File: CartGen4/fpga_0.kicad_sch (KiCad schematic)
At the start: 12 parts, among them U9 LFXP2-8E-5MN132C

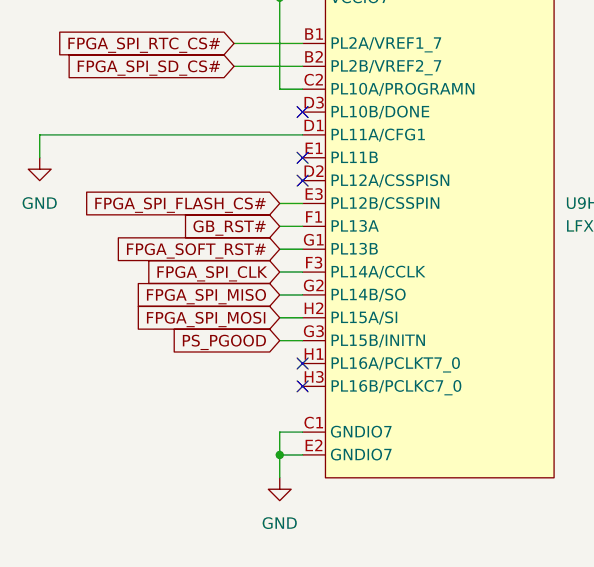
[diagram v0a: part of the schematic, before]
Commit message: Wired SPI bus
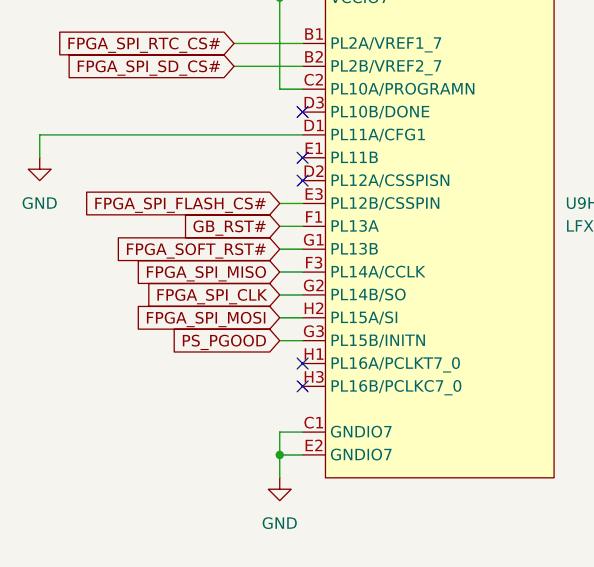
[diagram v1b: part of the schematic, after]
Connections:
- net FPGA_SPI_CLK: now also U9.G2 (PL14B/SO); no longer U9.F3 (PL14A/CCLK)
- net FPGA_SPI_MISO: now also U9.F3 (PL14A/CCLK); no longer U9.G2 (PL14B/SO)
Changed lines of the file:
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@@
+    )
+  )
+  (global_label "FPGA_SPI_CLK" (shape input) (at 53.34 82.55 180) (fields_autoplaced)
+    (effects (font (size 1.27 1.27)) (justify right))
+    (property "Intersheet References" "${INTERSHEET_REFS}" (id 0) (at 37.6221 82.4706 0)
+      (effects (font (size 1.27 1.27)) (justify right) hide)
     )
   )
@@
     )
   )
-  (global_label "FPGA_SPI_CLK" (shape input) (at 53.34 80.01 180) (fields_autoplaced)
-    (effects (font (size 1.27 1.27)) (justify right))
-    (property "Intersheet References" "${INTERSHEET_REFS}" (id 0) (at 37.6221 79.9306 0)
-      (effects (font (size 1.27 1.27)) (justify right) hide)
-    )
-  )
   (global_label "FPGA_SPI_FLASH_CS#" (shape input) (at 53.34 72.39 180) (fields_autoplaced)
     (effects (font (size 1.27 1.27)) (justify right))
@@
     )
   )
+  (global_label "FPGA_SPI_MISO" (shape input) (at 53.34 80.01 180) (fields_autoplaced)
+    (effects (font (size 1.27 1.27)) (justify right))
+    (property "Intersheet References" "${INTERSHEET_REFS}" (id 0) (at 36.594 79.9306 0)
+      (effects (font (size 1.27 1.27)) (justify right) hide)
+    )
+  )
   (global_label "RAM_ADV#" (shape input) (at 143.51 48.26 180) (fields_autoplaced)
     (effects (font (size 1.27 1.27)) (justify right))
@@
     (effects (font (size 1.27 1.27)) (justify right))
     (property "Intersheet References" "${INTERSHEET_REFS}" (id 0) (at 205.0807 65.9606 0)
-      (effects (font (size 1.27 1.27)) (justify right) hide)
-    )
-  )
-  (global_label "FPGA_SPI_MISO" (shape input) (at 53.34 82.55 180) (fields_autoplaced)
-    (effects (font (size 1.27 1.27)) (justify right))
-    (property "Intersheet References" "${INTERSHEET_REFS}" (id 0) (at 36.594 82.4706 0)
       (effects (font (size 1.27 1.27)) (justify right) hide)
     )
@@
   (symbol (lib_id "power:+1V2") (at 139.7 123.19 0) (unit 1)
     (in_bom yes) (on_board yes) (fields_autoplaced)
-    (property "Reference" "#PWR?" (id 0) (at 139.7 127 0)
+    (property "Reference" "#PWR0103" (id 0) (at 139.7 127 0)
       (effects (font (size 1.27 1.27)) hide)
     )
@@
   (symbol (lib_id "power:+3V3") (at 214.63 123.19 0) (unit 1)
     (in_bom yes) (on_board yes) (fields_autoplaced)
-    (property "Reference" "#PWR?" (id 0) (at 214.63 127 0)
+    (property "Reference" "#PWR0106" (id 0) (at 214.63 127 0)
       (effects (font (size 1.27 1.27)) hide)
     )
@@
   (symbol (lib_id "power:GND") (at 198.12 140.97 0) (unit 1)
     (in_bom yes) (on_board yes) (fields_autoplaced)
-    (property "Reference" "#PWR?" (id 0) (at 198.12 147.32 0)
+    (property "Reference" "#PWR0104" (id 0) (at 198.12 147.32 0)
       (effects (font (size 1.27 1.27)) hide)
     )
@@
   (symbol (lib_id "power:+1V8") (at 185.42 123.19 0) (unit 1)
     (in_bom yes) (on_board yes) (fields_autoplaced)
-    (property "Reference" "#PWR?" (id 0) (at 185.42 127 0)
+    (property "Reference" "#PWR0105" (id 0) (at 185.42 127 0)
       (effects (font (size 1.27 1.27)) hide)
     )
@@
   (symbol (lib_id "power:GND") (at 265.43 140.97 0) (unit 1)
     (in_bom yes) (on_board yes) (fields_autoplaced)
-    (property "Reference" "#PWR?" (id 0) (at 265.43 147.32 0)
-      (effects (font (size 1.27 1.27)) hide)
-    )
+    (property "Reference" "#PWR0107" (id 0) (at 265.43 147.32 0)
+      (effects (font (size 1.27 1.27)) hide)
+    )

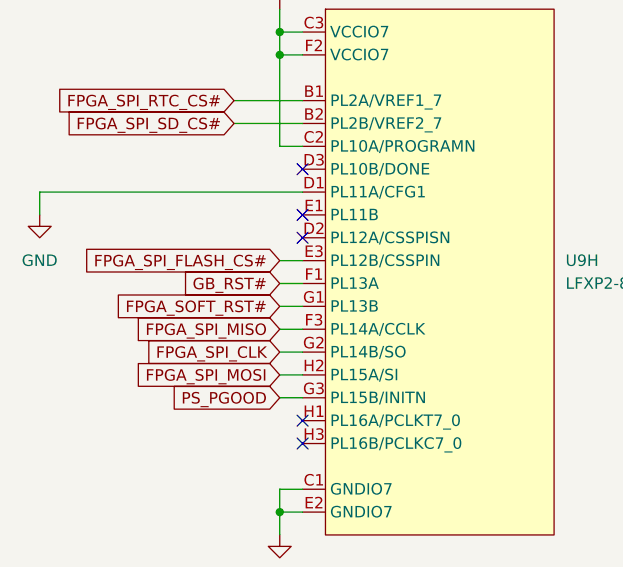
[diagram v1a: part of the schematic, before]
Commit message: Wired general purpose signals
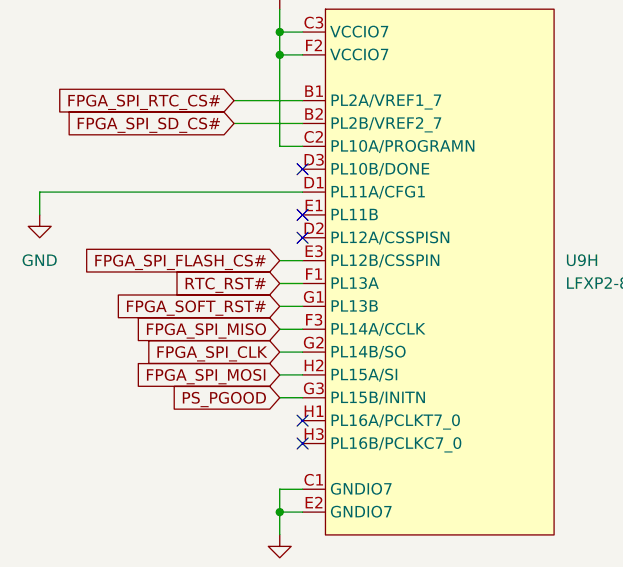
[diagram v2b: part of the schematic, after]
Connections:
- net GB_RST# renamed RTC_RST#
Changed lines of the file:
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@@
-    )
-  )
-  (global_label "GB_RST#" (shape input) (at 53.34 74.93 180) (fields_autoplaced)
-    (effects (font (size 1.27 1.27)) (justify right))
-    (property "Intersheet References" "${INTERSHEET_REFS}" (id 0) (at 42.7021 75.0094 0)
-      (effects (font (size 1.27 1.27)) (justify right) hide)
     )
   )
@@
       (effects (font (size 1.27 1.27)) (justify right) hide)
     )
+  )
+  (global_label "RTC_RST#" (shape input) (at 53.34 74.93 180) (fields_autoplaced)
+    (effects (font (size 1.27 1.27)) (justify right))
+    (property "Intersheet References" "${INTERSHEET_REFS}" (id 0) (at 41.7345 74.8506 0)
+      (effects (font (size 1.27 1.27)) (justify right) hide)
+    )

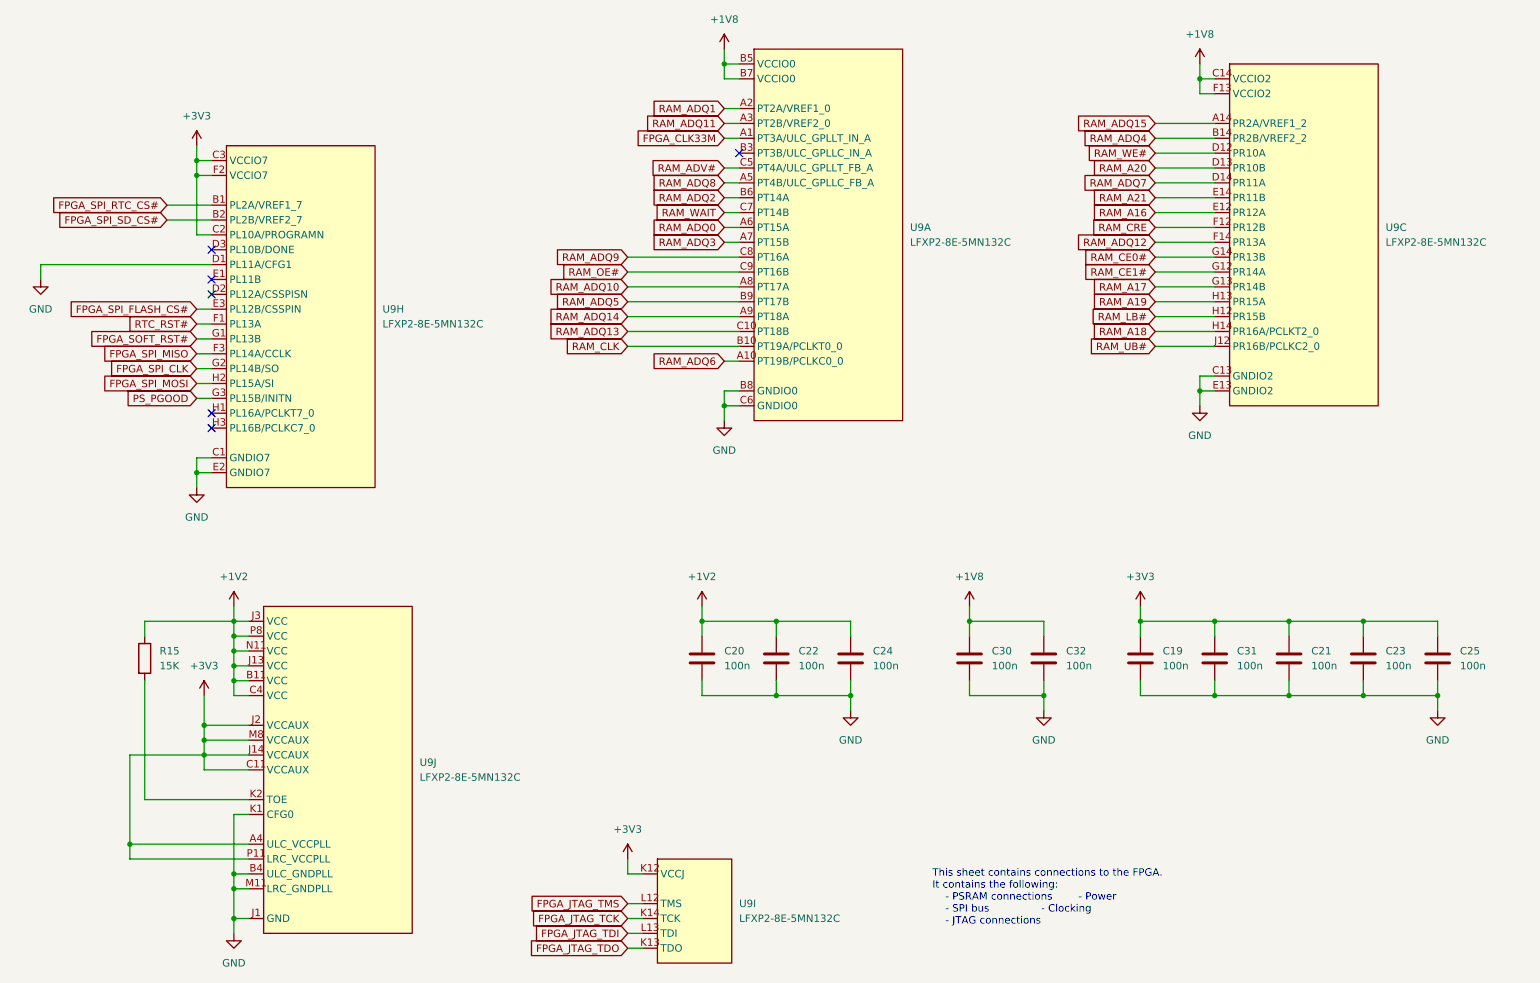
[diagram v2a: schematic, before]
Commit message: Rerouted some RAM and GB CTRL traces
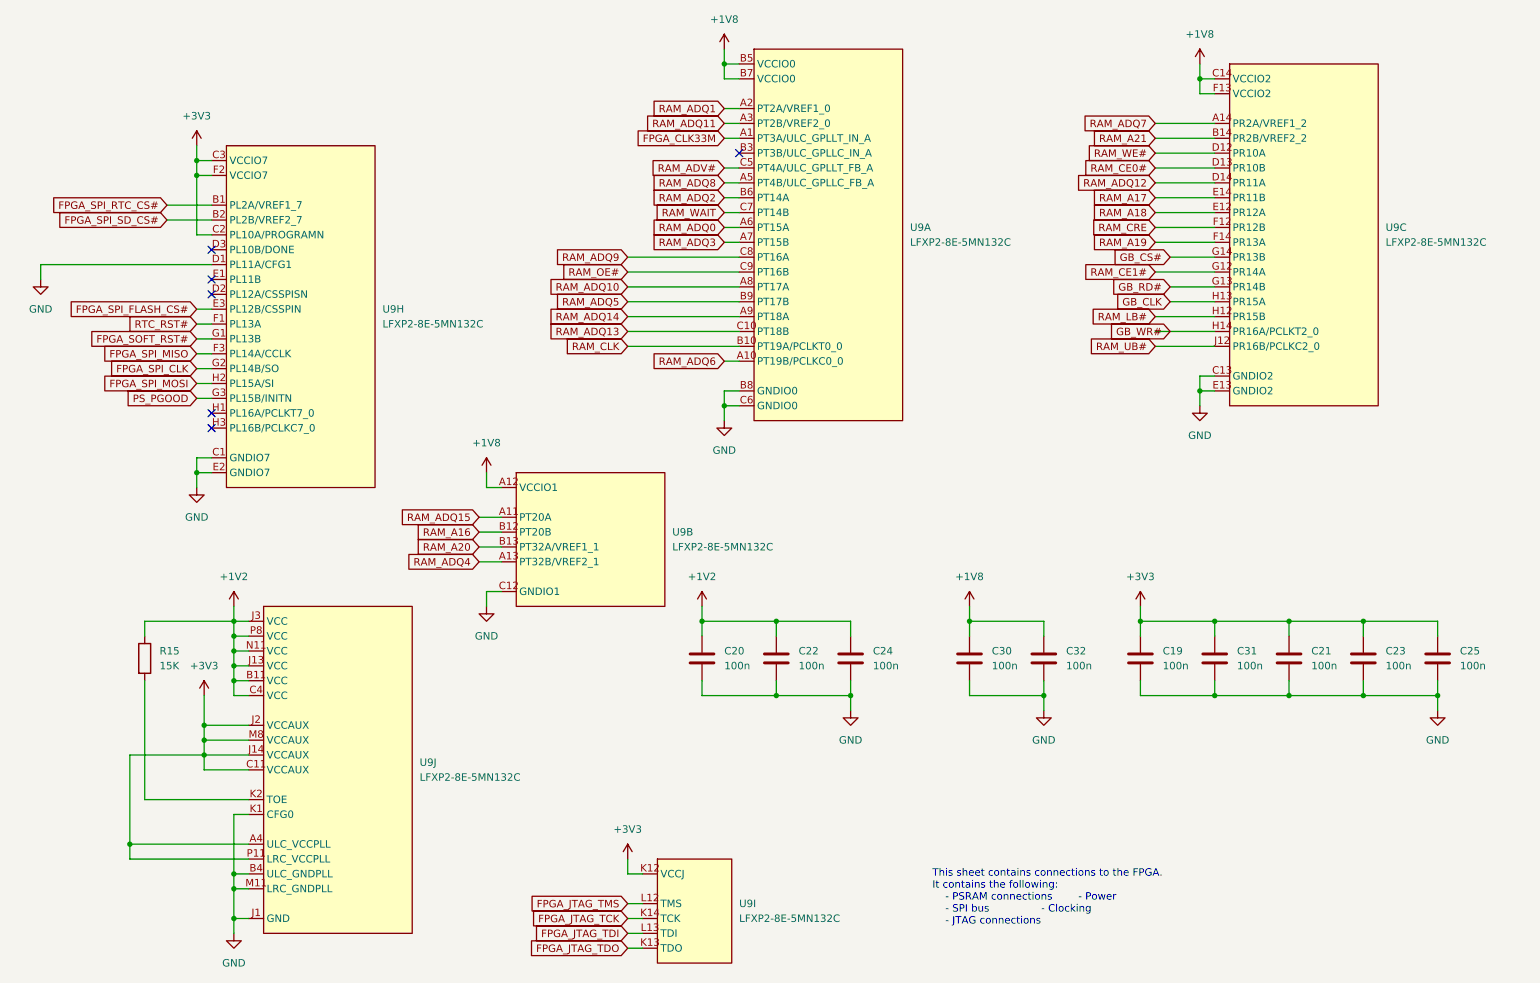
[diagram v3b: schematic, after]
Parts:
- added unit 2 of U9
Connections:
- net +1V8: now also U9.A12 (VCCIO1)
- net GND: now also U9.C12 (GNDIO1)
- net RAM_A16: now also U9.B12 (PT20B); no longer U9.E12 (PR12A)
- net RAM_A17: now also U9.E14 (PR11B); no longer U9.G13 (PR14B)
- net RAM_A18: now also U9.E12 (PR12A); no longer U9.H14 (PR16A/PCLKT2_0)
- net RAM_A19: now also U9.F14 (PR13A); no longer U9.H13 (PR15A)
- net RAM_A20: now also U9.B13 (PT32A/VREF1_1); no longer U9.D13 (PR10B)
- net RAM_A21: now also U9.B14 (PR2B/VREF2_2); no longer U9.E14 (PR11B)
- net RAM_ADQ12: now also U9.D14 (PR11A); no longer U9.F14 (PR13A)
- net RAM_ADQ15: now also U9.A11 (PT20A); no longer U9.A14 (PR2A/VREF1_2)
- net RAM_ADQ4: now also U9.A13 (PT32B/VREF2_1); no longer U9.B14 (PR2B/VREF2_2)
- net RAM_ADQ7: now also U9.A14 (PR2A/VREF1_2); no longer U9.D14 (PR11A)
- net RAM_CE0#: now also U9.D13 (PR10B); no longer U9.G14 (PR13B)
- new net GB_CLK: U9.H13 (PR15A)
- new net GB_CS#: U9.G14 (PR13B)
- new net GB_RD#: U9.G13 (PR14B)
- new net GB_WR#: U9.H14 (PR16A/PCLKT2_0)

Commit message: Added external test header to schematic
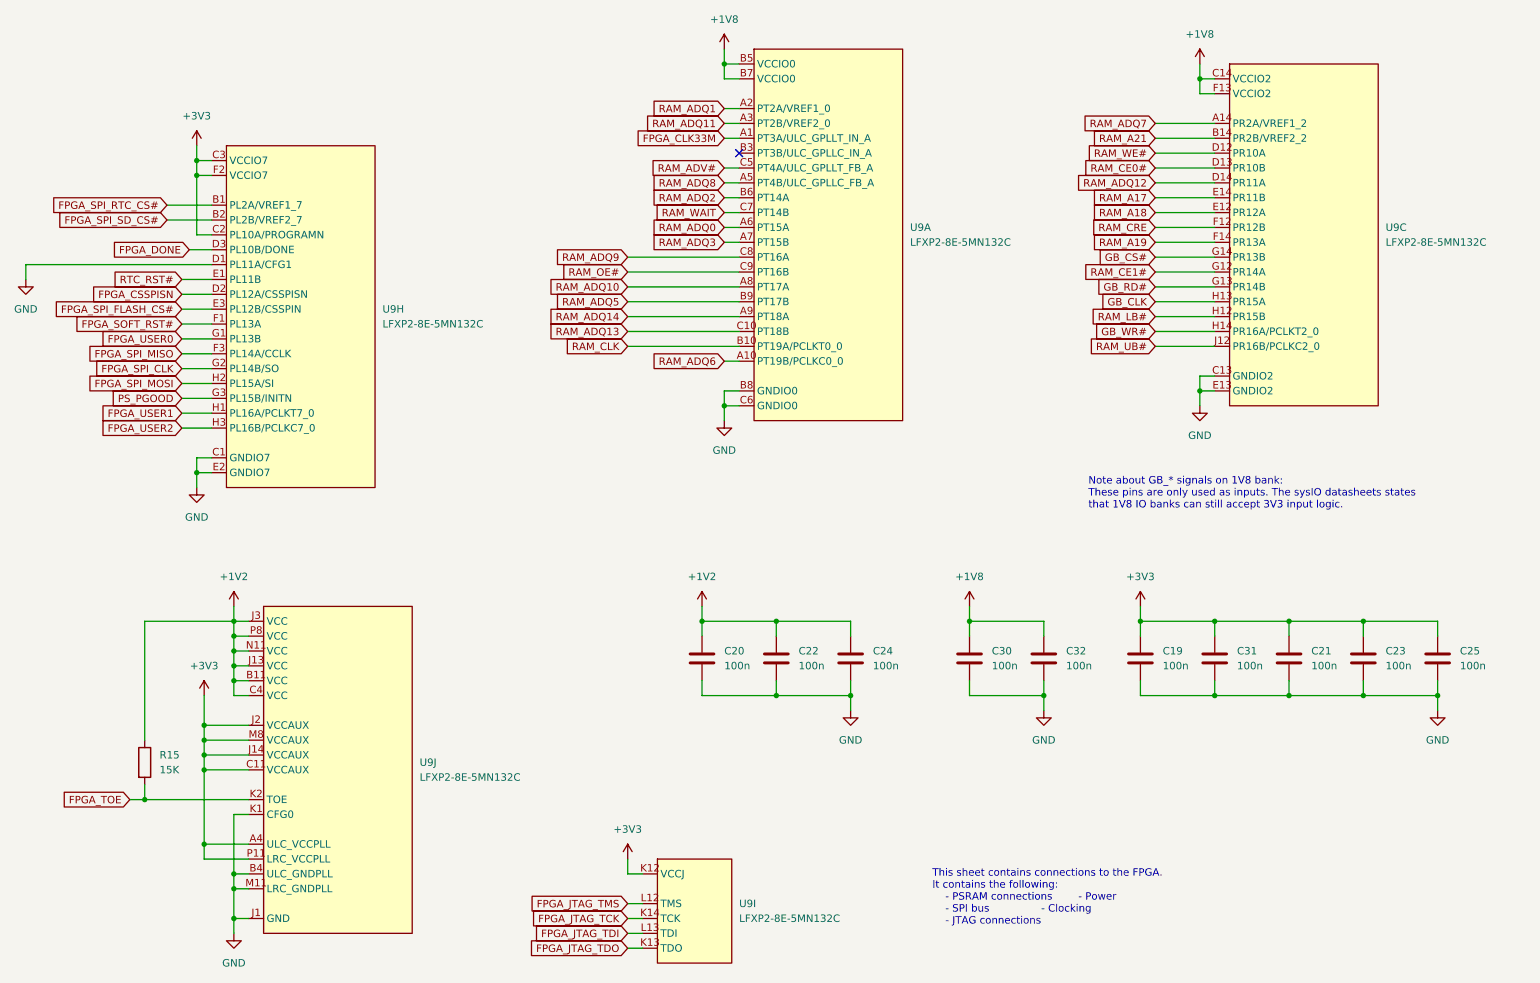
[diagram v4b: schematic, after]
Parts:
- removed unit 2 of U9
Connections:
- net FPGA_SOFT_RST#: now also U9.F1 (PL13A); no longer U9.G1 (PL13B)
- net RTC_RST#: now also U9.E1 (PL11B); no longer U9.F1 (PL13A)
- net FPGA_TOE: now reaches R15.2, U9.K2 (TOE)
- net FPGA_CSSPISN: now reaches U9.D2 (PL12A/CSSPISN)
- net FPGA_DONE: now reaches U9.D3 (PL10B/DONE)
- net FPGA_USER1: now reaches U9.H1 (PL16A/PCLKT7_0)
- net FPGA_USER2: now reaches U9.H3 (PL16B/PCLKC7_0)
- new net FPGA_USER0: U9.G1 (PL13B)
- no-connect marks 6 -> 1
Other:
- note added: "Note about GB_* signals on 1V8 bank: These pins are only used as inputs. The sysIO datasheets states that 1V8 IO banks can still accept 3V3 input logic."
- moved on the sheet: R15

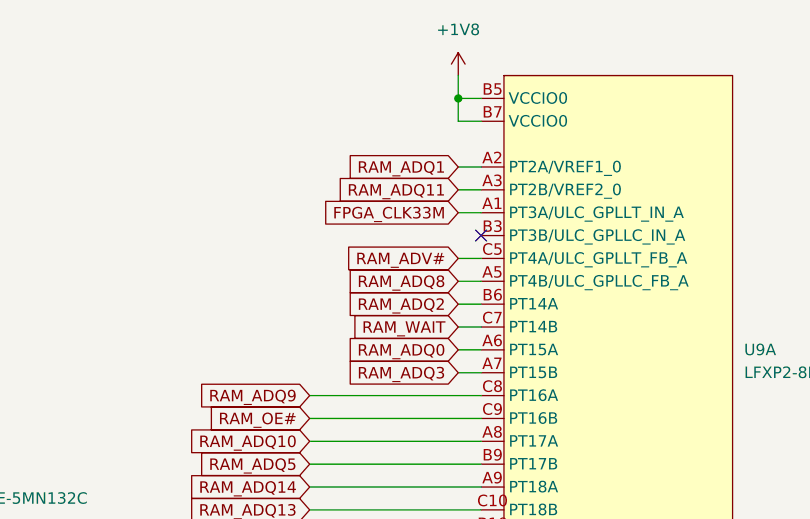
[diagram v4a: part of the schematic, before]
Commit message: Routed almost forgotten GB_BUS_EN
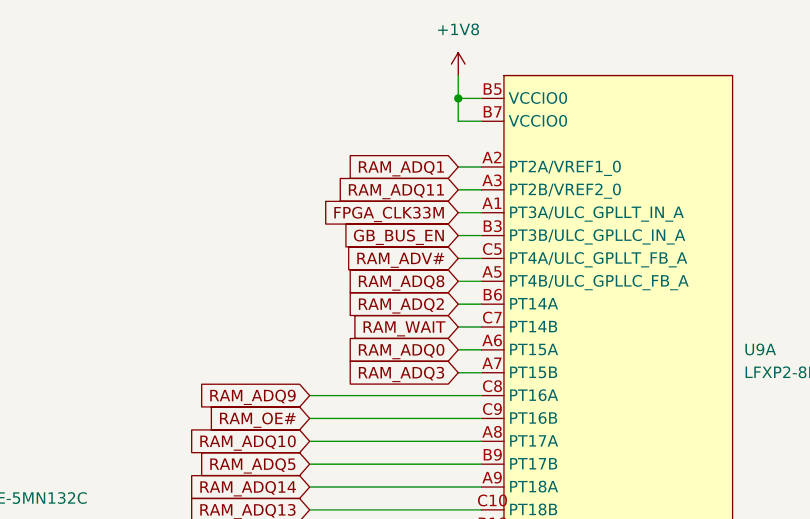
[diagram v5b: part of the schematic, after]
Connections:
- net GB_BUS_EN: now reaches U9.B3 (PT3B/ULC_GPLLC_IN_A)
- no-connect marks 1 -> 0
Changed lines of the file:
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@@
   (junction (at 240.03 138.43) (diameter 0) (color 0 0 0 0)
   )
-  (no_connect (at 146.05 45.72))
   (wire (pts (xy 50.8 77.47) (xy 55.88 77.47))
     (stroke (width 0) (type default) (color 0 0 0 0))
@@
   )
   (wire (pts (xy 59.69 128.27) (xy 59.69 125.73))
+    (stroke (width 0) (type default) (color 0 0 0 0))
+  )
+  (wire (pts (xy 143.51 45.72) (xy 146.05 45.72))
     (stroke (width 0) (type default) (color 0 0 0 0))
   )
@@
       (effects (font (size 1.27 1.27)) (justify right) hide)
     )
+  )
+  (global_label "GB_BUS_EN" (shape input) (at 143.51 45.72 180) (fields_autoplaced)
+    (effects (font (size 1.27 1.27)) (justify right))
+    (property "Intersheet References" "${INTERSHEET_REFS}" (id 0) (at 130.3321 45.6406 0)
+      (effects (font (size 1.27 1.27)) (justify right) hide)
+    )
